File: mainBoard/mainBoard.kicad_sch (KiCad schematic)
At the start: 47 parts, among them J1 XT60PW-M, J2 XT60PW-M, J21 B2B-PH_K, J22 Conn_01x02, J3 XT30PW-M, J4 XT30PW-M, J5 Barrel_Jack, J6 XT30U_F, Q1 FQD11P06TM, Q2 FQD11P06TM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

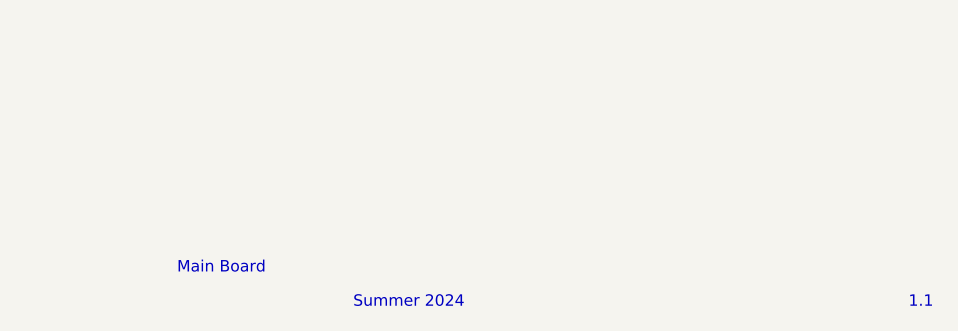
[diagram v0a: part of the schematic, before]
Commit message: Updated schematic sheet to have proper name, date, orgnization, and note
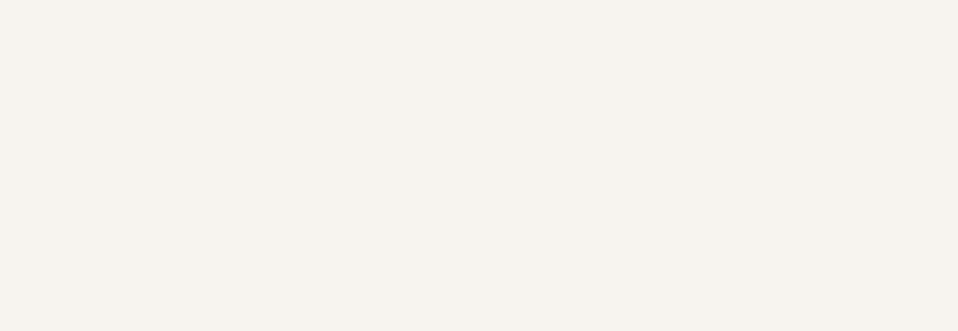
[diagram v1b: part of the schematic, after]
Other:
- note removed: "1.1"
- note removed: "Main Board"
- note removed: "Summer 2024"
- company: (none) -> GRR
- title: (none) -> Main Board 2024
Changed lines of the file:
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@@
 	(generator_version "8.0")
 	(paper "A4")
+	(title_block
+		(title "Main Board 2024")
+		(rev "1.1")
+		(company "GRR")
+		(comment 1 "Currently WIP")
+	)
 	(junction
 		(at 160.02 53.34)
@@
 		(fill
 			(type none)
-		)
-	)
-	(text "1.1"
-		(exclude_from_sim no)
-		(at 269.748 193.548 0)
-		(effects
-			(font
-				(size 1.27 1.27)
-			)
 		)
 	)
@@
 		(exclude_from_sim no)
 		(at 186.182 36.83 0)
-		(effects
-			(font
-				(size 1.27 1.27)
-			)
-		)
-	)
-	(text "Main Board"
-		(exclude_from_sim no)
-		(at 192.024 189.738 0)
 		(effects
 			(font
@@
 		(effects
 			(font
-				(size 1.27 1.27)
-			)
-		)
-	)
-	(text "Summer 2024"
-		(exclude_from_sim no)
-		(at 212.852 193.548 0)
-		(effects
-			(font

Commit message: more notes
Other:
- note added: "Note: Current draw of ALL LEDs should be 20ma. Use this in calculating resistor values"
- title: Main Board 2024 -> Main Board 2024-2025
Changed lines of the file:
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@@
 	(paper "A4")
 	(title_block
-		(title "Main Board 2024")
+		(title "Main Board 2024-2025")
 		(rev "1.1")
 		(company "GRR")
@@
 	)
 	(junction
-		(at 120.65 45.72)
+		(at 120.65 43.18)
 		(diameter 0)
 		(color 0 0 0 0)
@@
 	(wire
 		(pts
+			(xy 120.65 41.91) (xy 120.65 43.18)
+		)
+		(stroke
+			(width 0)
+			(type default)
+		)
+	)
+	(wire
+		(pts
 			(xy 160.02 62.23) (xy 160.02 60.96)
 		)
@@
 	(wire
 		(pts
-			(xy 120.65 45.72) (xy 120.65 53.34)
+			(xy 120.65 43.18) (xy 120.65 53.34)
 		)
 		(stroke
@@
 	(wire
 		(pts
-			(xy 125.73 43.18) (xy 129.54 43.18)
-		)
-		(stroke
-			(width 0)
-			(type default)
-		)
-	)
-	(wire
-		(pts
 			(xy 204.47 102.87) (xy 200.66 102.87)
 		)
@@
 	(wire
 		(pts
-			(xy 120.65 45.72) (xy 125.73 45.72)
+			(xy 120.65 43.18) (xy 129.54 43.18)
 		)
 		(stroke
@@
 	(wire
 		(pts
-			(xy 120.65 44.45) (xy 120.65 45.72)
-		)
-		(stroke
-			(width 0)
-			(type default)
-		)
-	)
-	(wire
-		(pts
 			(xy 120.65 53.34) (xy 128.27 53.34)
 		)
@@
 	(wire
 		(pts
-			(xy 125.73 45.72) (xy 125.73 43.18)
-		)
-		(stroke
-			(width 0)
-			(type default)
-		)
-	)
-	(wire
-		(pts
 			(xy 208.28 67.31) (xy 208.28 66.04)
 		)
@@
 	)
 	(rectangle
-		(start 116.84 38.1)
-		(end 259.08 78.74)
+		(start 116.84 36.83)
+		(end 259.08 77.47)
 		(stroke
 			(width 0)
@@
 	(text "12V to 5V, 3A"
 		(exclude_from_sim no)
-		(at 186.182 36.83 0)
+		(at 186.182 35.814 0)
 		(effects
 			(font
@@
 		)
 	)
+	(text "Note: Current draw of ALL LEDs should be 20ma.\nUse this in calculating resistor values"
+		(exclude_from_sim no)
+		(at 209.296 24.892 0)
+		(effects
+			(font
+				(size 2 2)
+			)
+		)
+	)
 	(text "Note: EN floating to turn on as soon as it gets power"
 		(exclude_from_sim no)
@@
 	(symbol
 		(lib_id "power:+12V")
-		(at 120.65 44.45 0)
+		(at 120.65 41.91 0)
 		(unit 1)
 		(exclude_from_sim no)
@@
 		(dnp no)
 		(property "Reference" "#PWR014"
-			(at 120.65 48.26 0)
+			(at 120.65 45.72 0)
 			(effects
 				(font
@@
 		)
 		(property "Value" "+12V"
-			(at 120.65 40.64 0)
+			(at 120.65 38.1 0)
 			(effects
 				(font
@@
 		)
 		(property "Footprint" ""
-			(at 120.65 44.45 0)
+			(at 120.65 41.91 0)
 			(effects
 				(font
@@
 		)
 		(property "Datasheet" ""
-			(at 120.65 44.45 0)
+			(at 120.65 41.91 0)
 			(effects
 				(font
@@
 		)
 		(property "Description" "Power symbol creates a global label with name \"+12V\""
-			(at 120.65 44.45 0)
+			(at 120.65 41.91 0)
 			(effects
 				(font

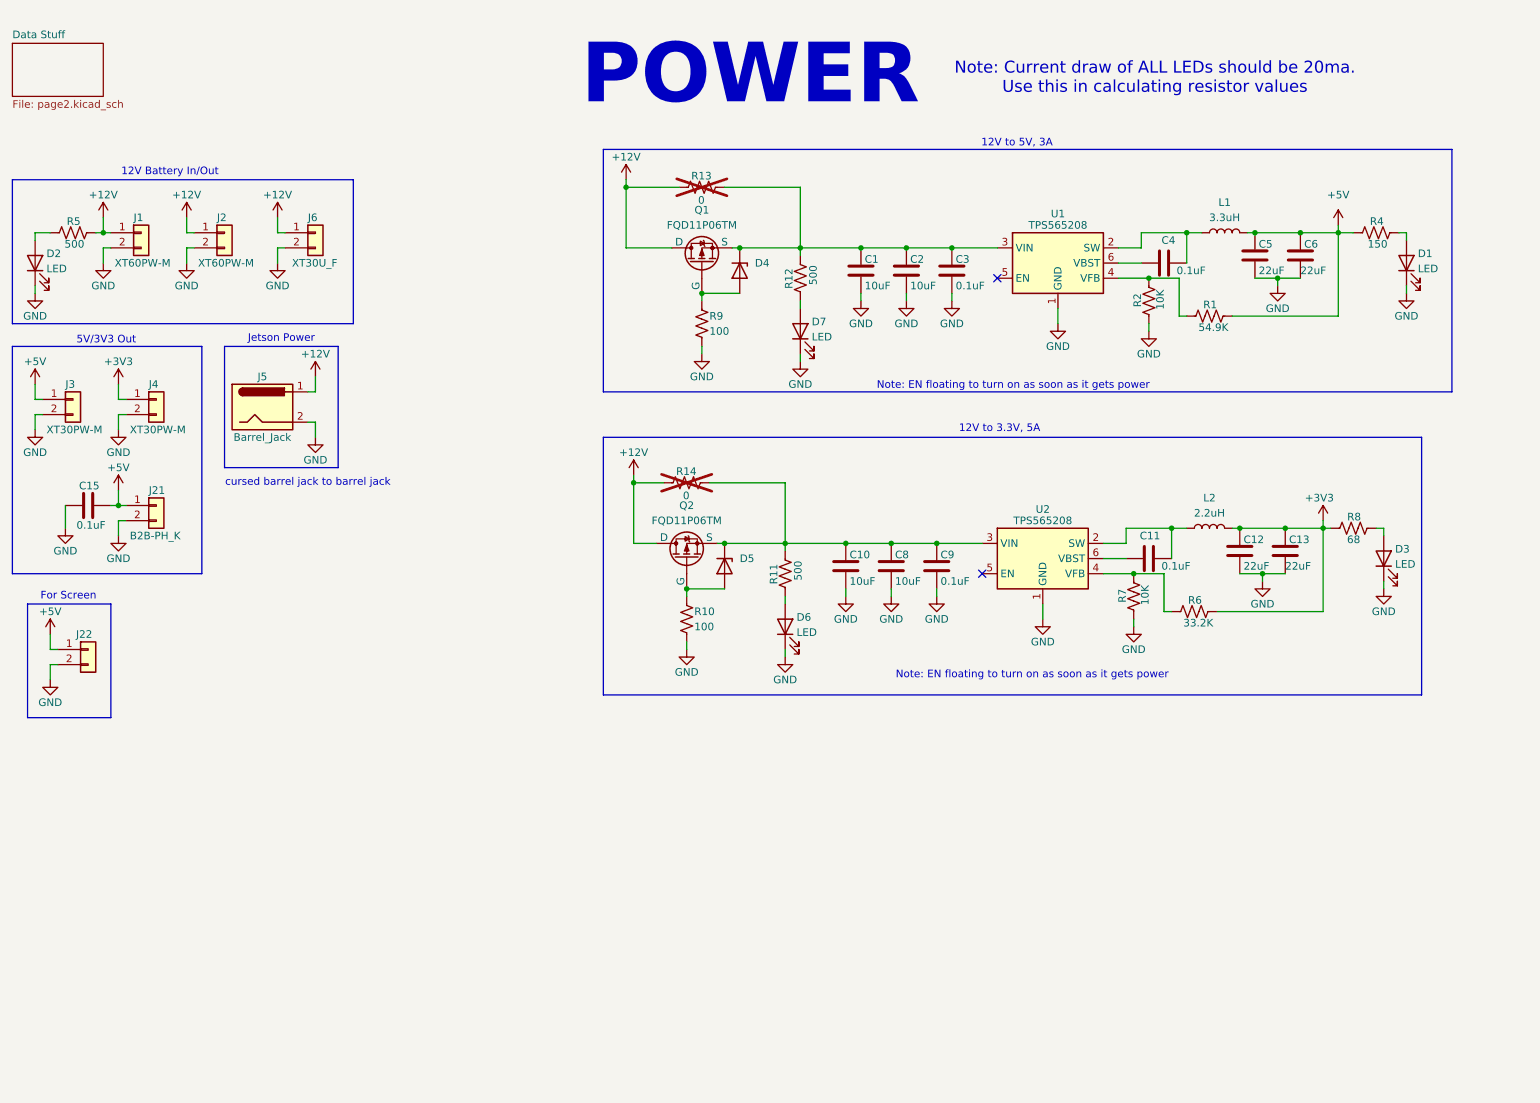
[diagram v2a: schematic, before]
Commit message: layed out mainboard as tano reccomended, added mounting holes, images, and new step file
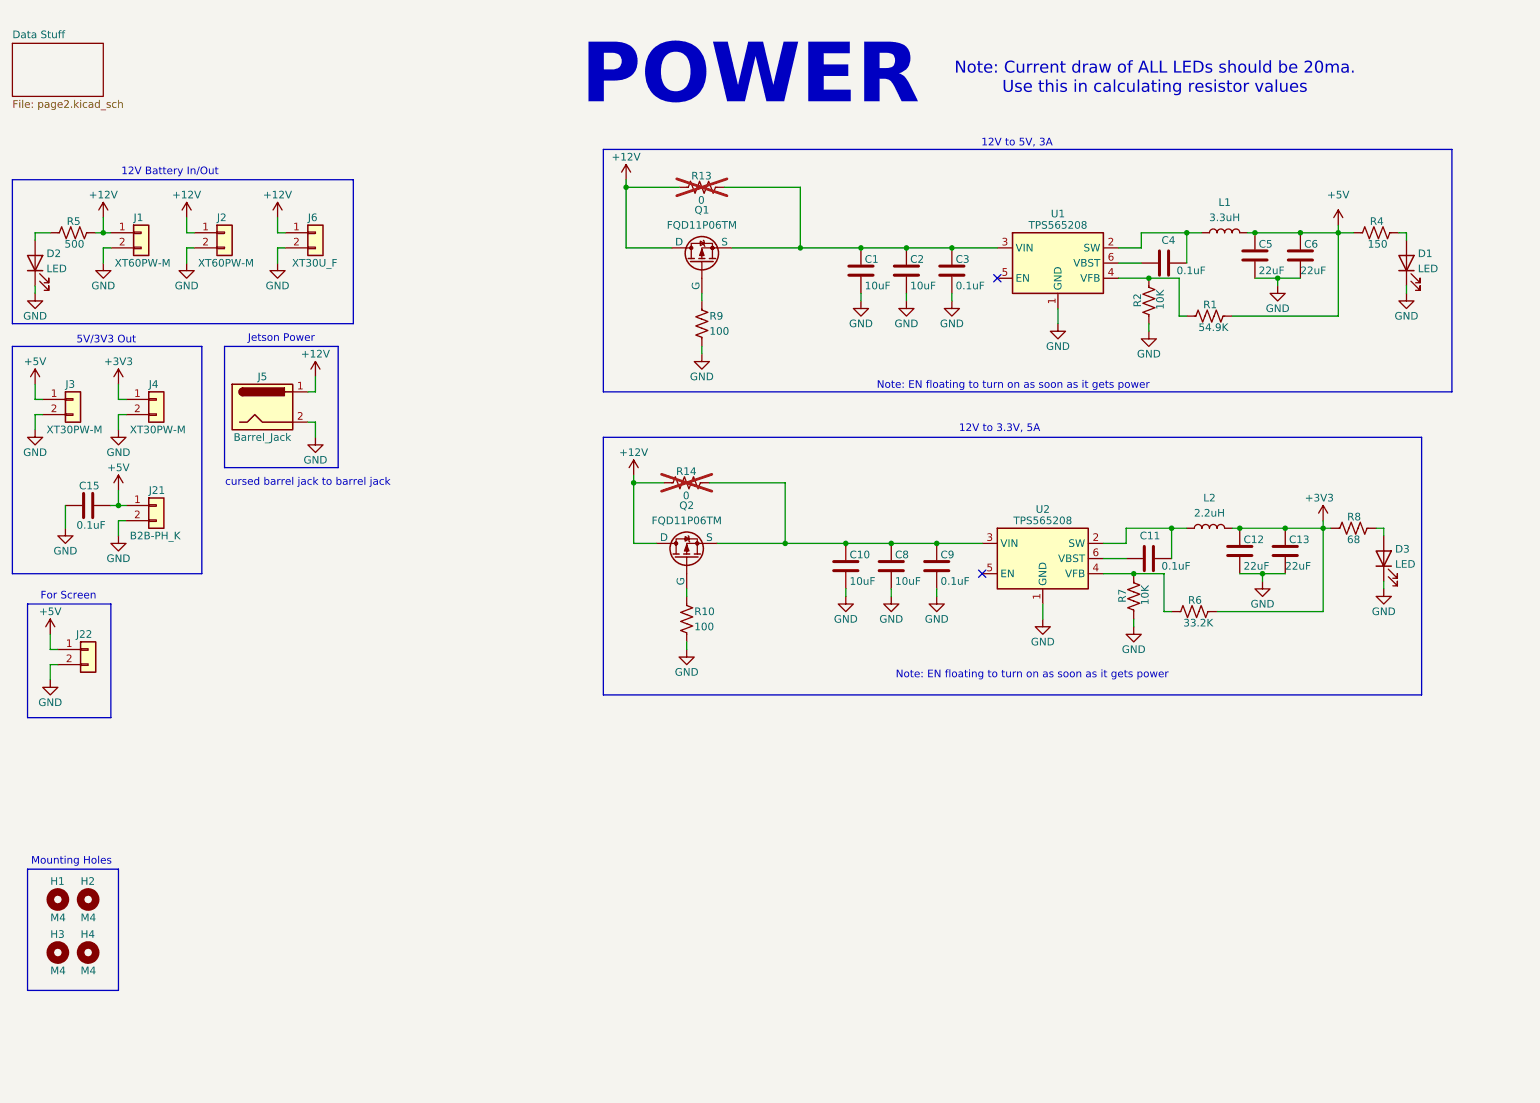
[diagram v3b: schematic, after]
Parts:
- removed D4, D5: 1SMA5925BT3G, Diode_SMD:D_SMA_Handsoldering, symbol Device:D_Zener
- removed D6, D7: LED, Diode_SMD:D_0805_2012Metric_Pad1.15x1.40mm_HandSolder, symbol Device:LED
- removed R11, R12: 500, Resistor_SMD:R_0805_2012Metric_Pad1.20x1.40mm_HandSolder, symbol Device:R_US
- added H1, H2, H3, H4: M4, MountingHole:MountingHole_4.3mm_M4_DIN965, symbol Mechanical:MountingHole
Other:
- note added: "Mounting Holes"

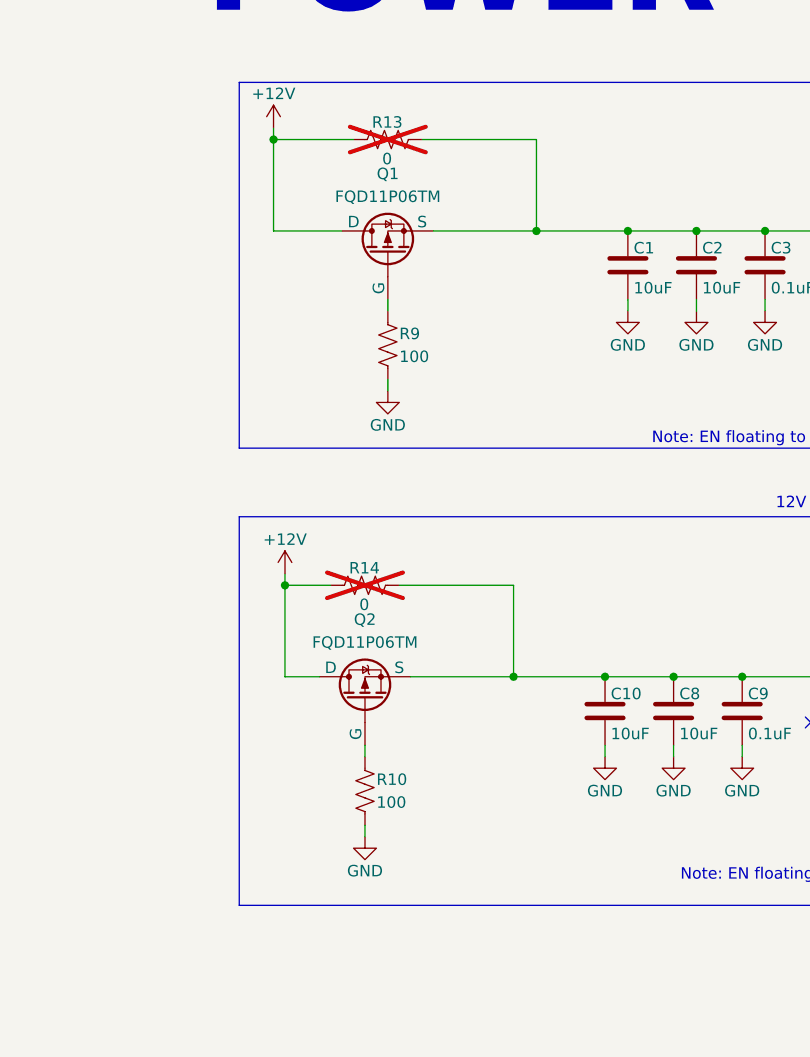
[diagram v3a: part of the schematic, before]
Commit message: Fixed error with PNP mosfet
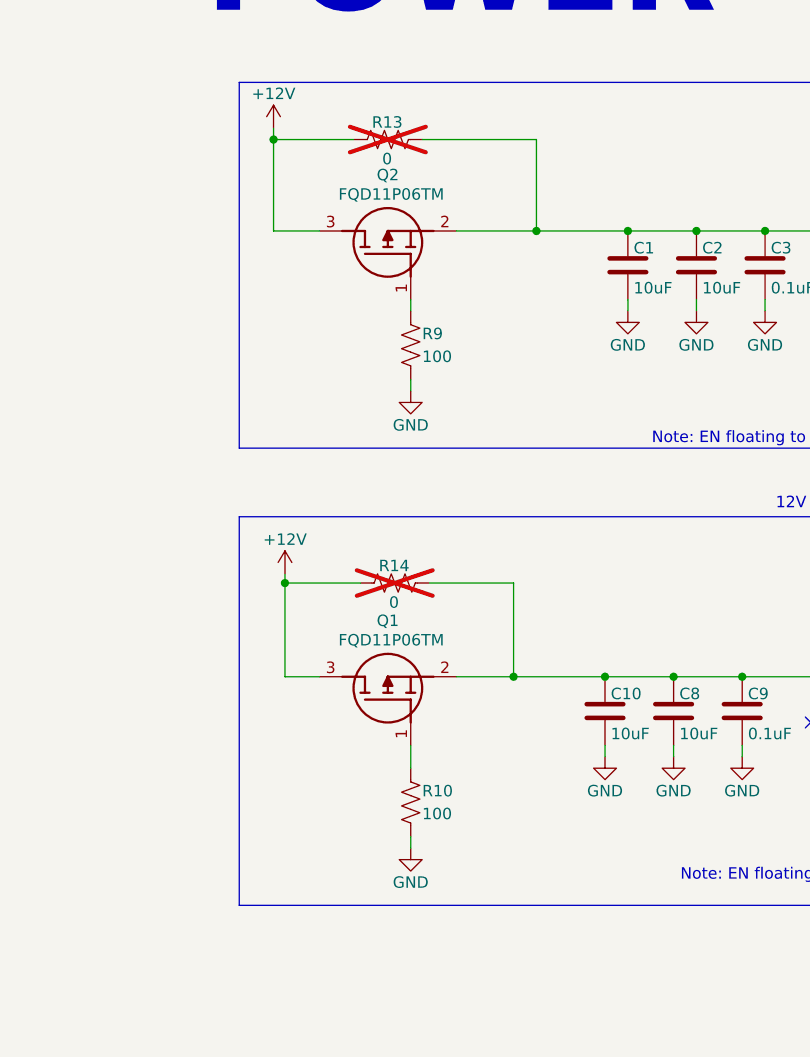
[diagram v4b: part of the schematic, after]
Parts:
- removed Q1, Q2: FQD11P06TM, Package_TO_SOT_SMD:TO-252-3_TabPin2, symbol Simulation_SPICE:PMOS
- added Q1, Q2: FQD11P06TM, Package_TO_SOT_SMD:TO-252-2, symbol FQD11P06TM:FQD11P06TM
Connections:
- net +12V: now also Q1.3 (D), Q2.3 (D)
- net at C1.1, C2.1, C3.1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: now also Q2.2 (S)
- net at C10.1, C8.1, C9.1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: now also Q1.2 (S)
- net at R9.1: now also Q2.1 (G)
- net at R10.1: now also Q1.1 (G)
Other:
- moved on the sheet: R14

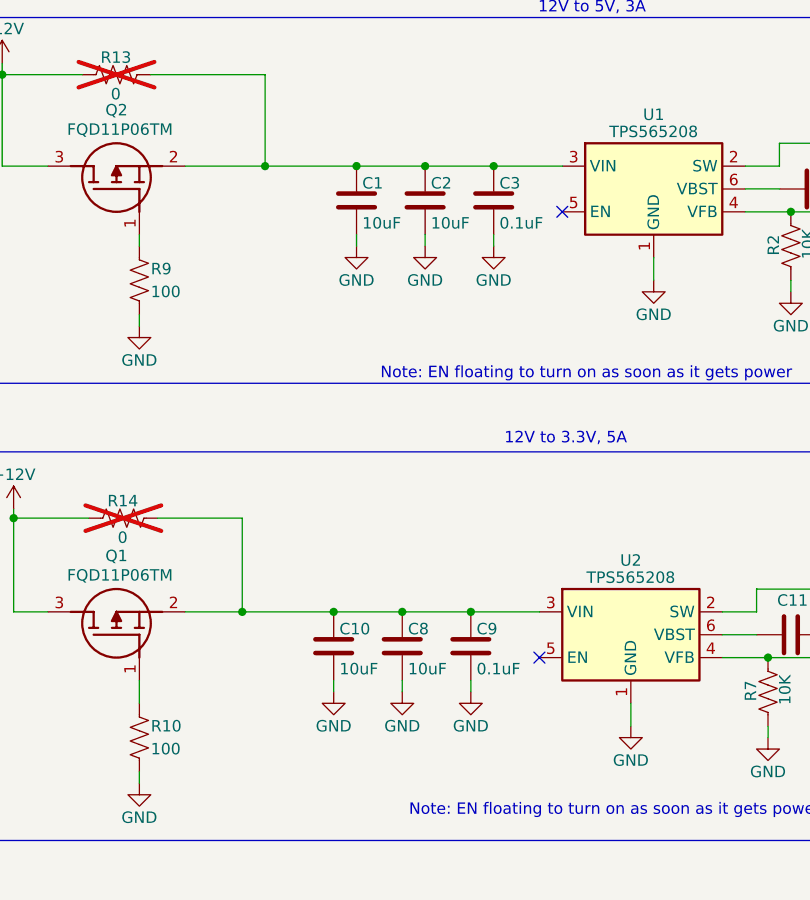
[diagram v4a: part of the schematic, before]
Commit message: Reviewed PCB with justin and made changes
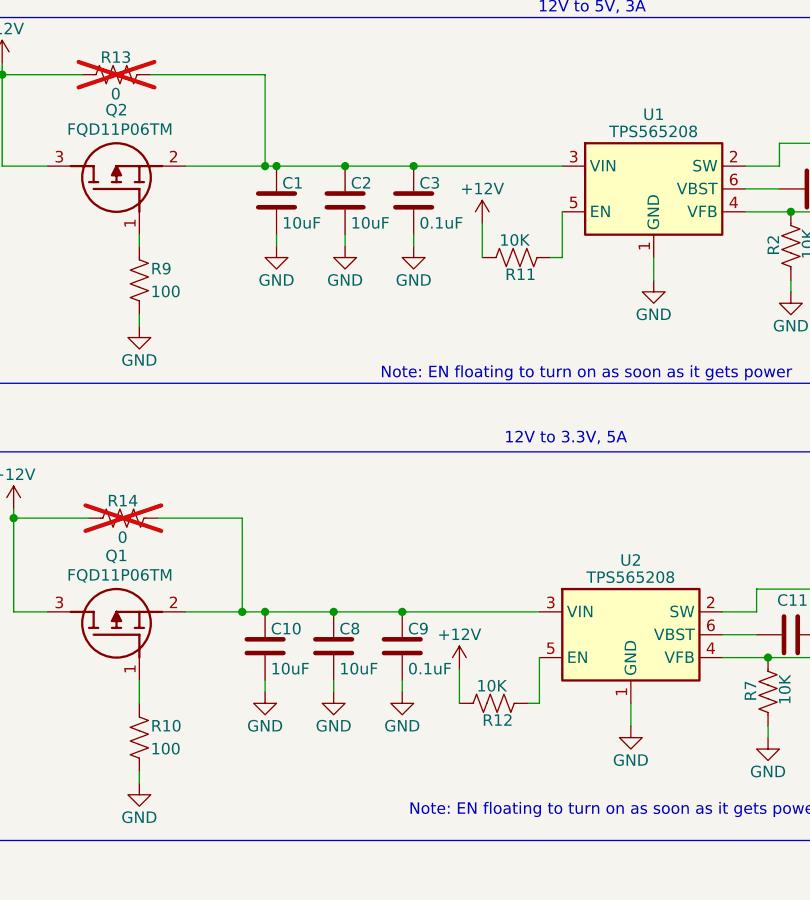
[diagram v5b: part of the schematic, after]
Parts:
- added R11, R12: 10K, Resistor_SMD:R_0805_2012Metric_Pad1.20x1.40mm_HandSolder, symbol Device:R_US
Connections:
- net +12V: now also R11.2, R12.2
- net at U2.5 (EN): now also R12.1
- net at U1.5 (EN): now also R11.1
- no-connect marks 2 -> 0
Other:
- moved on the sheet: C1, C10, C2, C3, C8, C9
